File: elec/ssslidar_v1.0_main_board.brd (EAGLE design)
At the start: 29 x 42 mm, 62 parts, among them IC1 MIC5504-2.8YM5, IC2 MIC5504-2.8YM5, J1 DXLD_EXT_W_HOLES, K1 BUTTON-2P-REINFORCE-3100060P1, P10 PIN_SMD_1X1.6, P11 PIN_SMD_1X1.6, P12 PIN_SMD_1X1.6, P14 PIN_SMD_1X1.6, P15 PIN_SMD_1X1.6, P2 PIN_SMD_1X1.6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

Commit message: Finalized V1.0.
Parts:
- added U$4: (no value), SparkFun-Aesthetics:OSHW-LOGO-S
- moved U$3 33.4 mm to (4.55, 41.2)
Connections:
- net DXL<MCU: now also J1.10
- net DXL>MCU: now also J1.9
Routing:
- net DXL>MCU: track 24.6 -> 32.0 mm
- net DXL<MCU: track 25.2 -> 29.2 mm
- net GND: vias 31 -> 32
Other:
- board text added: "X"
- board text added: "Y"
- board text added: "Z"
- board text removed: "TODO connect dxld !!!"
- board text removed: "TODO orientation IMU"
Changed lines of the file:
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@@
 <grid distance="0.05" unitdist="mm" unit="mm" style="dots" multiple="1" display="yes" altdistance="0.025" altunitdist="inch" altunit="inch"/>
 <layers>
-<layer number="1" name="Top" color="4" fill="1" visible="yes" active="yes"/>
+<layer number="1" name="Top" color="4" fill="1" visible="no" active="yes"/>
 <layer number="2" name="Route2" color="1" fill="3" visible="no" active="yes"/>
 <layer number="3" name="Route3" color="4" fill="3" visible="no" active="yes"/>
@@
 <circle x="23" y="10" radius="2" width="0.1" layer="42"/>
 <circle x="5" y="37.05" radius="2" width="0.1" layer="42"/>
-<text x="26.1" y="39.95" size="1" layer="21" font="vector" ratio="17" rot="R135">PWR</text>
+<text x="25.9" y="40.15" size="1" layer="21" font="vector" ratio="17" rot="SR135">PWR</text>
 <dimension x1="0.5" y1="30" x2="29.5" y2="30" x3="15" y3="45.3" textsize="1" textratio="17" layer="47"/>
 <dimension x1="15" y1="43.5" x2="15" y2="1.5" x3="-0.8" y3="22.5" textsize="1" textratio="17" layer="47"/>
@@
 <wire x1="18" y1="4.5" x2="18.3" y2="4.9" width="0.15" layer="21"/>
 <wire x1="18.3" y1="4.9" x2="18.75" y2="5" width="0.15" layer="21"/>
-<text x="3.75" y="24.1" size="1.2" layer="21" font="vector" ratio="17">C</text>
-<text x="21.2" y="31.85" size="1.2" layer="21" font="vector" ratio="17">B</text>
-<text x="19.15" y="12.1" size="1.2" layer="21" font="vector" ratio="17">A</text>
+<text x="5.05" y="24.15" size="1.2" layer="21" font="vector" ratio="17" rot="R90">C</text>
+<text x="21.45" y="31.9" size="1.2" layer="21" font="vector" ratio="17" rot="R90">B</text>
+<text x="20.1" y="12.15" size="1.2" layer="21" font="vector" ratio="17" rot="R90">A</text>
 <text x="16.7" y="15.35" size="0.9" layer="21" font="vector" ratio="17" rot="R285">PWR</text>
 <text x="21.05" y="28.9" size="0.9" layer="21" font="vector" ratio="17" rot="R45">SIG</text>
 <text x="6.7" y="26.2" size="0.9" layer="21" font="vector" ratio="17" rot="R165">SIG</text>
 <text x="26.85" y="23.1" size="1.3" layer="21" font="vector" ratio="17" rot="R90">V1.1</text>
-<text x="21.076771875" y="26.368196875" size="1" layer="22" font="vector" ratio="17" rot="SMR0">20160910</text>
+<text x="20.376771875" y="26.268196875" size="1" layer="22" font="vector" ratio="17" rot="SMR0">20160910</text>
 <text x="24.5" y="14.25" size="0.9" layer="22" font="vector" ratio="17" rot="SMR270">V</text>
 <text x="25.05" y="15.6" size="0.9" layer="22" font="vector" ratio="17" rot="SMR270">!R</text>
@@
 <wire x1="25.55" y1="16.8" x2="25.2" y2="16.1" width="0.15" layer="22"/>
 <wire x1="25.2" y1="16.1" x2="25.3" y2="15.9" width="0.15" layer="22"/>
-<text x="11.95" y="14.2" size="0.9" layer="22" font="vector" ratio="17" rot="MR0">2</text>
-<text x="19.9" y="9.3" size="0.9" layer="22" font="vector" ratio="17" rot="MR0">1</text>
-<text x="10.15" y="9.2" size="0.9" layer="21" font="vector" ratio="17" rot="SMR180">3</text>
+<text x="12.25" y="14.85" size="0.9" layer="22" font="vector" ratio="17" rot="SMR270">2</text>
+<text x="20.05" y="9.6" size="0.9" layer="22" font="vector" ratio="17" rot="SMR270">1</text>
+<text x="10.65" y="6.35" size="0.9" layer="21" font="vector" ratio="17" rot="SMR90">3</text>
 <circle x="16.65" y="2.75" radius="0.25" width="0" layer="21"/>
 <text x="7.418196875" y="34.623228125" size="1" layer="22" font="vector" ratio="17" rot="SMR90">DXLD</text>
@@
 <circle x="15.25" y="24.65" radius="0.25" width="0" layer="22"/>
 <circle x="17.35" y="6.25" radius="0.25" width="0" layer="22"/>
-<text x="0.65" y="44.85" size="1.778" layer="1" font="vector" ratio="15">TODO connect dxld !!!</text>
-<text x="32.5" y="25.25" size="1.778" layer="21" font="vector" rot="R90">TODO orientation IMU</text>
+<text x="10.25" y="32.75" size="0.9" layer="22" font="vector" ratio="17" rot="MR90">X</text>
+<text x="10.95" y="30.85" size="0.9" layer="22" font="vector" ratio="17" rot="MR90">Y</text>
+<text x="9.4" y="30.5" size="0.9" layer="22" font="vector" ratio="17" rot="MR90">Z</text>
+<wire x1="9.85" y1="32.4" x2="9.85" y2="33.15" width="0.2" layer="22"/>
+<wire x1="9.85" y1="33.15" x2="9.85" y2="33.55" width="0.2" layer="22"/>
+<wire x1="9.85" y1="33.55" x2="10.1" y2="33.15" width="0.2" layer="22"/>
+<wire x1="9.6" y1="33.15" x2="9.85" y2="33.55" width="0.2" layer="22"/>
+<wire x1="10.1" y1="33.15" x2="9.85" y2="33.15" width="0.2" layer="22"/>
+<wire x1="9.85" y1="33.15" x2="9.6" y2="33.15" width="0.2" layer="22"/>
+<wire x1="10.4" y1="31.85" x2="11.15" y2="31.85" width="0.2" layer="22"/>
+<wire x1="11.15" y1="31.85" x2="11.55" y2="31.85" width="0.2" layer="22"/>
+<wire x1="11.55" y1="31.85" x2="11.15" y2="31.6" width="0.2" layer="22"/>
+<wire x1="11.15" y1="32.1" x2="11.55" y2="31.85" width="0.2" layer="22"/>
+<wire x1="11.15" y1="31.6" x2="11.15" y2="31.85" width="0.2" layer="22"/>
+<wire x1="11.15" y1="31.85" x2="11.15" y2="32.1" width="0.2" layer="22"/>
+<circle x="9.85" y="31.85" radius="0.2" width="0" layer="22"/>
+<circle x="9.85" y="31.85" radius="0.5" width="0.2" layer="22"/>
+<text x="15.45" y="33.05" size="0.9" layer="21" font="vector" ratio="17" rot="R90">X</text>
+<text x="16.85" y="31.4" size="0.9" layer="21" font="vector" ratio="17" rot="SR90">Y</text>
+<text x="15.45" y="29.45" size="0.9" layer="21" font="vector" ratio="17" rot="SR90">Z</text>
+<wire x1="15" y1="31.45" x2="15" y2="32.4" width="0.2" layer="21"/>
+<wire x1="15" y1="32.4" x2="15" y2="32.8" width="0.2" layer="21"/>
+<wire x1="15" y1="32.8" x2="14.75" y2="32.4" width="0.2" layer="21"/>
+<wire x1="15.25" y1="32.4" x2="15" y2="32.8" width="0.2" layer="21"/>
+<wire x1="14.75" y1="32.4" x2="15" y2="32.4" width="0.2" layer="21"/>
+<wire x1="15" y1="32.4" x2="15.25" y2="32.4" width="0.2" layer="21"/>
+<wire x1="15.55" y1="30.95" x2="16.3" y2="30.95" width="0.2" layer="21"/>
+<wire x1="16.3" y1="30.95" x2="16.7" y2="30.95" width="0.2" layer="21"/>
+<wire x1="16.7" y1="30.95" x2="16.3" y2="31.2" width="0.2" layer="21"/>
+<wire x1="16.3" y1="30.7" x2="16.7" y2="30.95" width="0.2" layer="21"/>
+<wire x1="16.3" y1="31.2" x2="16.3" y2="30.95" width="0.2" layer="21"/>
+<wire x1="16.3" y1="30.95" x2="16.3" y2="30.7" width="0.2" layer="21"/>
+<circle x="15" y="30.95" radius="0.5" width="0.2" layer="21"/>
+<wire x1="14.65" y1="31.3" x2="15.35" y2="30.6" width="0.2" layer="21"/>
+<wire x1="15.35" y1="31.3" x2="14.65" y2="30.6" width="0.2" layer="21"/>
 </plain>
 <attributes>
@@
 <element name="R4" library="Xevelabs" package="0402_N" value="TBD" x="24.8" y="20.65" rot="MR90"/>
 <element name="R6" library="Xevelabs" package="0402_N" value="TBD" x="25.9" y="20.65" rot="MR90"/>
-<element name="U$3" library="Xevelabs" package="XEVELABS_LOGO_S" value="" x="14.95" y="9.5"/>
+<element name="U$3" library="Xevelabs" package="XEVELABS_LOGO_S" value="" x="4.55" y="41.25"/>
 <element name="U6" library="mpu6000" package="QFN-24" value="MPU-6050" x="15" y="31" rot="MR270">
 <attribute name="DATASHEET" value="http://invensense.com/mems/gyro/documents/PS-MPU-6000A-00_v1.0.pdf" x="5.8" y="38.6" size="1.778" layer="28" rot="MR270" display="off"/>
@@
 <element name="C11" library="Xevelabs" package="0805_N" value="10uF" x="25.4" y="30.6" rot="MR0"/>
 <element name="C3" library="Xevelabs" package="0402_N" value="100nF" x="18.15" y="28.65" rot="MR90"/>
+<element name="U$4" library="SparkFun-Aesthetics" package="OSHW-LOGO-S" value="" x="15" y="8.15"/>
 </elements>
 <signals>
@@
 <via x="18" y="30.35" extent="1-16" drill="0.3"/>
 <via x="13.05" y="28.95" extent="1-16" drill="0.3"/>
+<via x="23" y="30.6" extent="1-16" drill="0.3"/>
 </signal>
 <signal name="SCL">
@@
 <wire x1="23.55" y1="16.55" x2="23.55" y2="27.85" width="0.15" layer="16"/>
 <wire x1="23.55" y1="27.85" x2="21.15" y2="30.25" width="0.15" layer="16"/>
-<wire x1="21.15" y1="30.25" x2="21.15" y2="31.6" width="0.15" layer="16"/>
+<wire x1="21.15" y1="30.25" x2="21.15" y2="32" width="0.15" layer="16"/>
+<contactref element="J1" pad="9"/>
+<wire x1="21.15" y1="32" x2="19.5" y2="33.65" width="0.15" layer="16"/>
+<wire x1="19.5" y1="33.65" x2="19.5" y2="36.54" width="0.15" layer="16"/>
+<wire x1="19.5" y1="36.54" x2="20.73" y2="37.77" width="0.15" layer="16"/>
 </signal>
 <signal name="DXL&lt;MCU">
@@
 <wire x1="23.9" y1="16.45" x2="23.9" y2="28" width="0.15" layer="16"/>
 <wire x1="23.9" y1="28" x2="21.5" y2="30.4" width="0.15" layer="16"/>
-<wire x1="21.5" y1="30.4" x2="21.5" y2="31.55" width="0.15" layer="16"/>
+<wire x1="21.5" y1="30.4" x2="21.5" y2="32.2" width="0.15" layer="16"/>
+<contactref element="J1" pad="10"/>
+<wire x1="21.5" y1="32.2" x2="20.7" y2="33" width="0.15" layer="16"/>
+<wire x1="20.7" y1="33" x2="20.7" y2="35.2" width="0.15" layer="16"/>
+<wire x1="20.7" y1="35.2" x2="20.73" y2="35.23" width="0.15" layer="16"/>
 </signal>
 <signal name="INT">

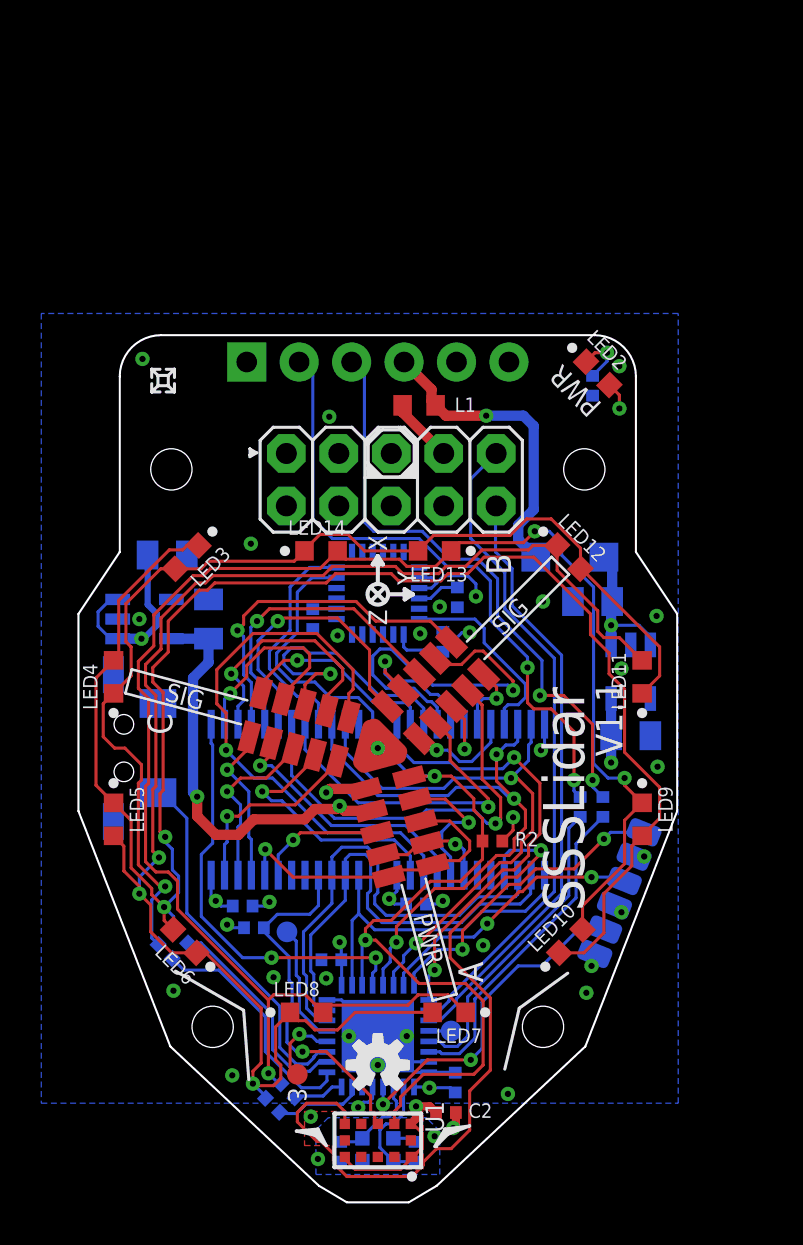
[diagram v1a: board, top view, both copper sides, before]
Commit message: Upadted blade footprint, put everything in v1.0
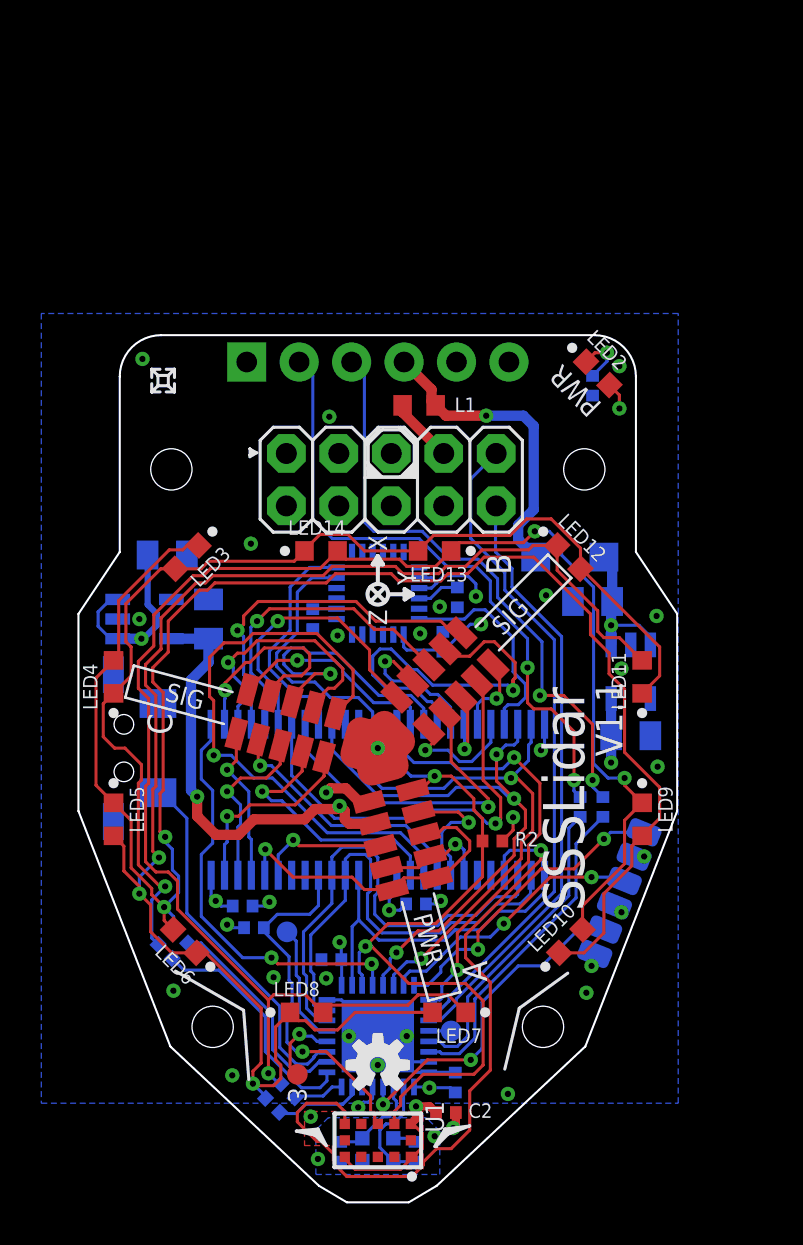
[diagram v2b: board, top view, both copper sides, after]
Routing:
- net VDD: track 26.2 -> 27.9 mm
- net F_INT2: track 27.1 -> 28.6 mm
- net GND: track 20.1 -> 21.1 mm, vias 32 -> 31
- net G_INT1: track 34.2 -> 33.2 mm
- net MPU_INT: track 9.53 -> 10.5 mm
- net B_INT2: track 18.5 -> 19.4 mm
- net VEE: track 52.7 -> 53.4 mm
- net F_SDA1: track 11.9 -> 12.6 mm
- net !MUX_EN: track 22.6 -> 23.3 mm
- net MUX_ADDR2: track 22.1 -> 22.8 mm
- net C_SDA1: track 9.53 -> 10.2 mm
- net MUX_ADDR0: track 29.3 -> 28.7 mm

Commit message: Aesthetic modifs
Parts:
- moved U$3 31.7 mm to (14.9, 11.3)
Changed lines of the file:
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@@
 <layer number="19" name="Unrouted" color="6" fill="1" visible="yes" active="yes"/>
 <layer number="20" name="Dimension" color="15" fill="1" visible="yes" active="yes"/>
-<layer number="21" name="tPlace" color="7" fill="1" visible="no" active="yes"/>
+<layer number="21" name="tPlace" color="7" fill="1" visible="yes" active="yes"/>
 <layer number="22" name="bPlace" color="7" fill="1" visible="no" active="yes"/>
-<layer number="23" name="tOrigins" color="15" fill="1" visible="no" active="yes"/>
+<layer number="23" name="tOrigins" color="15" fill="1" visible="yes" active="yes"/>
 <layer number="24" name="bOrigins" color="15" fill="1" visible="no" active="yes"/>
 <layer number="25" name="tNames" color="7" fill="1" visible="no" active="yes"/>
@@
 <layer number="27" name="tValues" color="7" fill="1" visible="no" active="yes"/>
 <layer number="28" name="bValues" color="7" fill="1" visible="no" active="yes"/>
-<layer number="29" name="tStop" color="7" fill="3" visible="no" active="yes"/>
+<layer number="29" name="tStop" color="7" fill="3" visible="yes" active="yes"/>
 <layer number="30" name="bStop" color="7" fill="6" visible="no" active="yes"/>
 <layer number="31" name="tCream" color="7" fill="4" visible="no" active="yes"/>
@@
 <dimension x1="0.5" y1="30" x2="29.5" y2="30" x3="15" y3="45.3" textsize="1" textratio="17" layer="47"/>
 <dimension x1="15" y1="43.5" x2="15" y2="1.5" x3="-0.8" y3="22.5" textsize="1" textratio="17" layer="47"/>
-<text x="25" y="15.6" size="2" layer="21" font="vector" ratio="17" rot="SR90">SSSLidar</text>
+<text x="13.9" y="40.8" size="1.5" layer="21" font="vector" ratio="17" rot="SR180">SSSLidar</text>
 <wire x1="5.2" y1="12.7" x2="8.5" y2="10.8" width="0.15" layer="21"/>
 <wire x1="8.5" y1="10.8" x2="8.75" y2="7.45" width="0.15" layer="21"/>
@@
 <text x="21.05" y="28.9" size="0.9" layer="21" font="vector" ratio="17" rot="R45">SIG</text>
 <text x="6.7" y="26.2" size="0.9" layer="21" font="vector" ratio="17" rot="R165">SIG</text>
-<text x="26.85" y="23.1" size="1.3" layer="21" font="vector" ratio="17" rot="R90">V1.1</text>
+<text x="7" y="42.65" size="1" layer="21" font="vector" ratio="17" rot="SR180">V1.1</text>
 <text x="20.376771875" y="26.268196875" size="1" layer="22" font="vector" ratio="17" rot="SMR0">20160910</text>
 <text x="24.5" y="14.25" size="0.9" layer="22" font="vector" ratio="17" rot="SMR270">V</text>
@@
 <element name="R4" library="Xevelabs" package="0402_N" value="TBD" x="24.8" y="20.65" rot="MR90"/>
 <element name="R6" library="Xevelabs" package="0402_N" value="TBD" x="25.9" y="20.65" rot="MR90"/>
-<element name="U$3" library="Xevelabs" package="XEVELABS_LOGO_S" value="" x="4.55" y="41.25"/>
+<element name="U$3" library="Xevelabs" package="XEVELABS_LOGO_S" value="" x="14.95" y="11.3"/>
 <element name="U6" library="mpu6000" package="QFN-24" value="MPU-6050" x="15" y="31" rot="MR270">
 <attribute name="DATASHEET" value="http://invensense.com/mems/gyro/documents/PS-MPU-6000A-00_v1.0.pdf" x="5.8" y="38.6" size="1.778" layer="28" rot="MR270" display="off"/>
